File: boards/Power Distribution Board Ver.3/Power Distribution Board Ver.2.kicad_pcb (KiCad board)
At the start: 4 copper layers, 127 x 127 mm, 95 parts, among them J1 Screw_Terminal_01x02, J2 Screw_Terminal_01x06, J3 Screw_Terminal_01x06, J4 Screw_Terminal_01x06, K1 Relay, K2 Relay, K3 Relay, K4 Relay, K5 Relay, K6 Relay, SW1 SW_Push_Open, U1 SIC431AED-T1-GE3, U2 SIC431AED-T1-GE3, U3 SIC431AED-T1-GE3

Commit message: schematic changes
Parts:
- removed D1, D2, D3, D4, D5, D6: type="D" model="DIODE" lib="", Package_TO_SOT_SMD:TO-263-2
- removed the G*** at (79.4, 48.4)
- removed J2, J3: Screw_Terminal_01x06, power_board_support:12V terminal block
- removed K1, K2, K3, K4, K5, K6: Relay, power_board_support:A10 Relay
- removed SW1: SW_Push_Open, power_board_support:E-Stop
- added F1: 0685P9200-01, IRIS:FUSC3215X83N, F.Cu at (61.2, 123.4)
- added F2: 0685P9200-01, IRIS:FUSC3215X83N, F.Cu at (51.3, 123.7)
- added F3: 0685P9200-01, IRIS:FUSC3215X83N, F.Cu at (41.2, 123.7)
- moved REF** 63.4 mm to (77.2, 130.7)
- moved REF** 63.3 mm to (76.7, 27.1)
- moved D9 13.0 mm to (35.8, 114.4)
- moved D8 12.6 mm to (67.6, 114.4)
- moved D7 12.4 mm to (52.1, 114.4)
- moved C11 9.38 mm to (42.8, 74.8)
- moved C13 9.38 mm to (72.0, 65.9)
- moved C14 9.38 mm to (50.9, 66.0)
- moved C15 9.38 mm to (33.0, 66.0)
- moved C17 9.38 mm to (50.5, 79.8)
- moved C22 9.38 mm to (57.0, 101.9)
- moved C27 9.38 mm to (77.3, 101.9)
- moved C31 9.38 mm to (77.3, 87.8)
- moved C39 9.38 mm to (38.8, 101.9)
- moved C4 9.38 mm to (75.3, 69.7)
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- renumbered C19~C25 to C19, C21 to C20, C28 to C21, C29 to C22, C30 to C23, C31 to C24, C32 to C25, C22 to C26, C19 to C27, C23 to C28, C24 to C29, C25 to C30, C26 to C31, C26~C32 to C32, C33~C39 to C39
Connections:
- D7 pad 2: /5V_OUT_2 -> Net-(D7-K)
- D8 pad 2: /5V_OUT_3 -> Net-(D8-K)
- D9 pad 2: /5V_OUT_1 -> Net-(D9-K)
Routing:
- net /E-stop: track 177.1 -> 0.00 mm
- net /12V_IN_2: track 19.3 -> 0.00 mm
- net /12V_IN_3: track 18.9 -> 0.00 mm
- net /12V_IN_1: track 18.9 -> 0.00 mm
- net /12V_IN_4: track 13.3 -> 0.00 mm
- net /12V_IN_6: track 13.3 -> 0.00 mm
- net /12V_IN_5: track 13.3 -> 0.00 mm
- net Net-(D7-K): track 0.00 -> 10.2 mm
- net Net-(D5-A): track 8.59 -> 0.00 mm
- net Net-(D3-A): track 8.59 -> 0.00 mm
- net Net-(D1-A): track 8.59 -> 0.00 mm
- net /5V_OUT_3: track 14.6 -> 6.69 mm
- net /5V_OUT_2: track 13.5 -> 6.41 mm
- net /5V_OUT_1: track 13.1 -> 6.41 mm
- net Net-(D2-A): track 5.68 -> 0.00 mm
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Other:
- board outline removed
- board text removed: "Buffett Lee, Emily Lory, Joseph Hanger, Henry Lin, Ben Saarva, Jakub Wojdyla, Wyatt Sturn, Miaomiao Jin"

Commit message: PCBPCB Schematics Done
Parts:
- removed D7, D8, D9: type="D" model="DIODE" lib="", Package_TO_SOT_SMD:TO-263-2
- moved G*** 25.4 mm to (75.5, 89.5)
- moved F1 22.4 mm to (74.0, 105.0)
- moved F2 18.9 mm to (54.1, 105.0)
- moved F3 18.2 mm to (42.0, 105.5)
- moved REF** 16.0 mm to (80.0, 115.0)
- moved REF** 15.7 mm to (26.0, 115.0)
- moved J4 15.3 mm to (56.5, 116.5)
- moved REF** 5.00 mm to (80.0, 30.9)
- moved REF** 3.98 mm to (26.0, 30.9)
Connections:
- C16 pad 1: Net-(D8-A) -> Net-(U1-VOUT)
- C17 pad 1: Net-(D7-A) -> Net-(U2-VOUT)
- C18 pad 1: Net-(D9-A) -> Net-(U3-VOUT)
- C19 pad 1: Net-(D7-A) -> Net-(U2-VOUT)
- C20 pad 1: Net-(D7-A) -> Net-(U2-VOUT)
- C21 pad 1: Net-(D7-A) -> Net-(U2-VOUT)
- C22 pad 1: Net-(D7-A) -> Net-(U2-VOUT)
- C23 pad 1: Net-(D7-A) -> Net-(U2-VOUT)
- C24 pad 1: Net-(D7-A) -> Net-(U2-VOUT)
- C25 pad 1: Net-(D7-A) -> Net-(U2-VOUT)
- C26 pad 1: Net-(D8-A) -> Net-(U1-VOUT)
- C27 pad 1: Net-(D8-A) -> Net-(U1-VOUT)
- C28 pad 1: Net-(D8-A) -> Net-(U1-VOUT)
- C29 pad 1: Net-(D8-A) -> Net-(U1-VOUT)
- C30 pad 1: Net-(D8-A) -> Net-(U1-VOUT)
- C31 pad 1: Net-(D8-A) -> Net-(U1-VOUT)
- C32 pad 1: Net-(D8-A) -> Net-(U1-VOUT)
- C33 pad 1: Net-(D9-A) -> Net-(U3-VOUT)
- C34 pad 1: Net-(D9-A) -> Net-(U3-VOUT)
- C35 pad 1: Net-(D9-A) -> Net-(U3-VOUT)
- C36 pad 1: Net-(D9-A) -> Net-(U3-VOUT)
- C37 pad 1: Net-(D9-A) -> Net-(U3-VOUT)
- C38 pad 1: Net-(D9-A) -> Net-(U3-VOUT)
- C39 pad 1: Net-(D9-A) -> Net-(U3-VOUT)
- F1 pad 1: Net-(D8-K) -> Net-(U1-VOUT)
- F2 pad 1: Net-(D7-K) -> Net-(U2-VOUT)
- F3 pad 1: Net-(D9-K) -> Net-(U3-VOUT)
- L1 pad 2: Net-(D8-A) -> Net-(U1-VOUT)
- L2 pad 2: Net-(D7-A) -> Net-(U2-VOUT)
- L3 pad 2: Net-(D9-A) -> Net-(U3-VOUT)
- R22 pad 2: Net-(D8-A) -> Net-(U1-VOUT)
- R23 pad 2: Net-(D7-A) -> Net-(U2-VOUT)
- R24 pad 2: Net-(D9-A) -> Net-(U3-VOUT)
- U1 pad 18: Net-(D8-A) -> Net-(U1-VOUT)
- U2 pad 18: Net-(D7-A) -> Net-(U2-VOUT)
- U3 pad 18: Net-(D9-A) -> Net-(U3-VOUT)
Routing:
- net Net-(D8-A): track 54.0 -> 0.00 mm
- net Net-(D9-A): track 48.9 -> 0.00 mm
- net Net-(U3-VOUT): track 0.00 -> 47.6 mm
- net Net-(D7-A): track 46.9 -> 0.00 mm
- net Net-(U1-VOUT): track 0.00 -> 46.0 mm
- net Net-(U2-VOUT): track 0.00 -> 42.4 mm
- net Net-(D7-K): track 10.2 -> 0.00 mm
- net /5V_OUT_3: track 6.69 -> 14.2 mm
- net Net-(D8-K): track 5.15 -> 0.00 mm
- net Net-(D9-K): track 5.03 -> 0.00 mm
- net /5V_OUT_1: track 6.41 -> 10.4 mm
- net /5V_OUT_2: track 6.41 -> 10.1 mm
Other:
- board text added: "+"
- board text added: "IRIS - XV PCBPCB Ver. 3 Rev. A Henry Lin, Rina Manxhuka, Janine Zhu Ben Saarva, Wyatt Sturn, Arnav Rajesh, Jakub Wojdyla, Hriday Shah, Sakshi Singh, Medha Hariharan, Terry Wang, Vimalnath Selvam, Nihar Koganti, Andrew Bajek, Nakul Sivaraj"

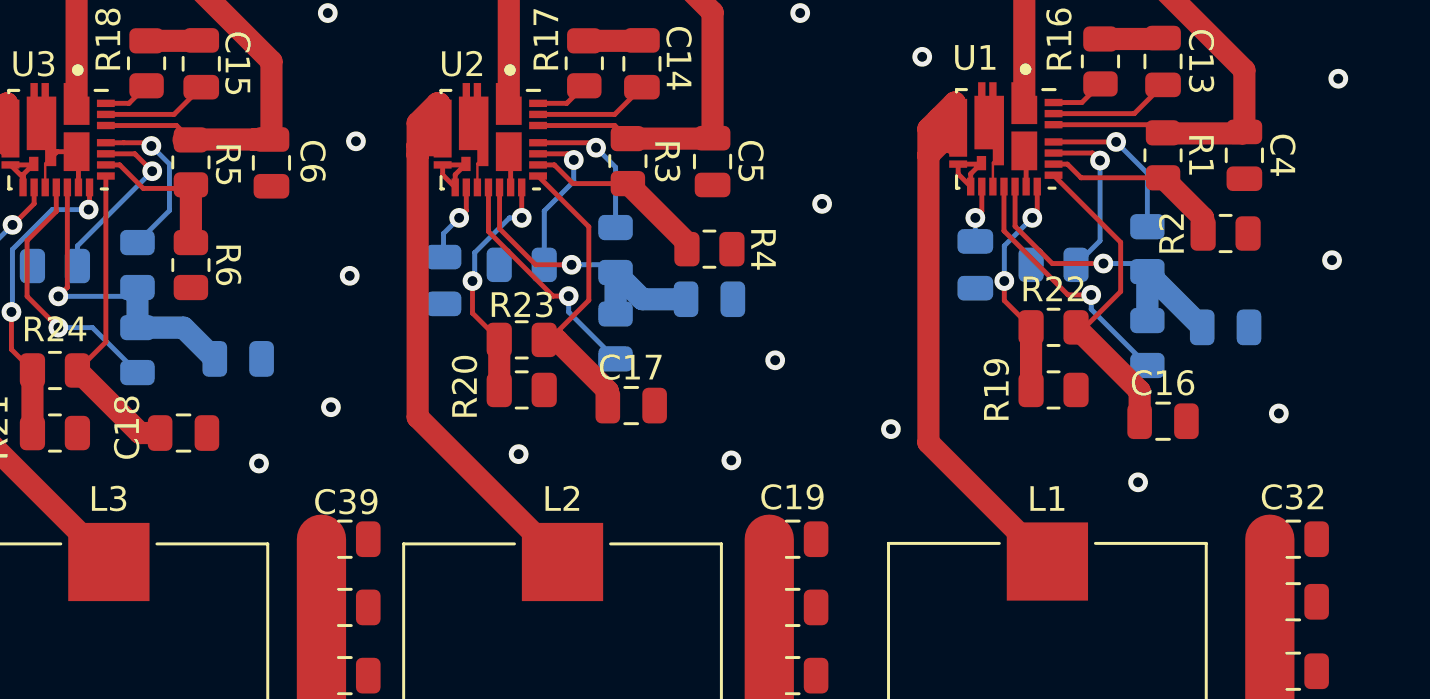
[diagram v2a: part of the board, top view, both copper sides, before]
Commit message: 12v relay footprint and updated board wiring
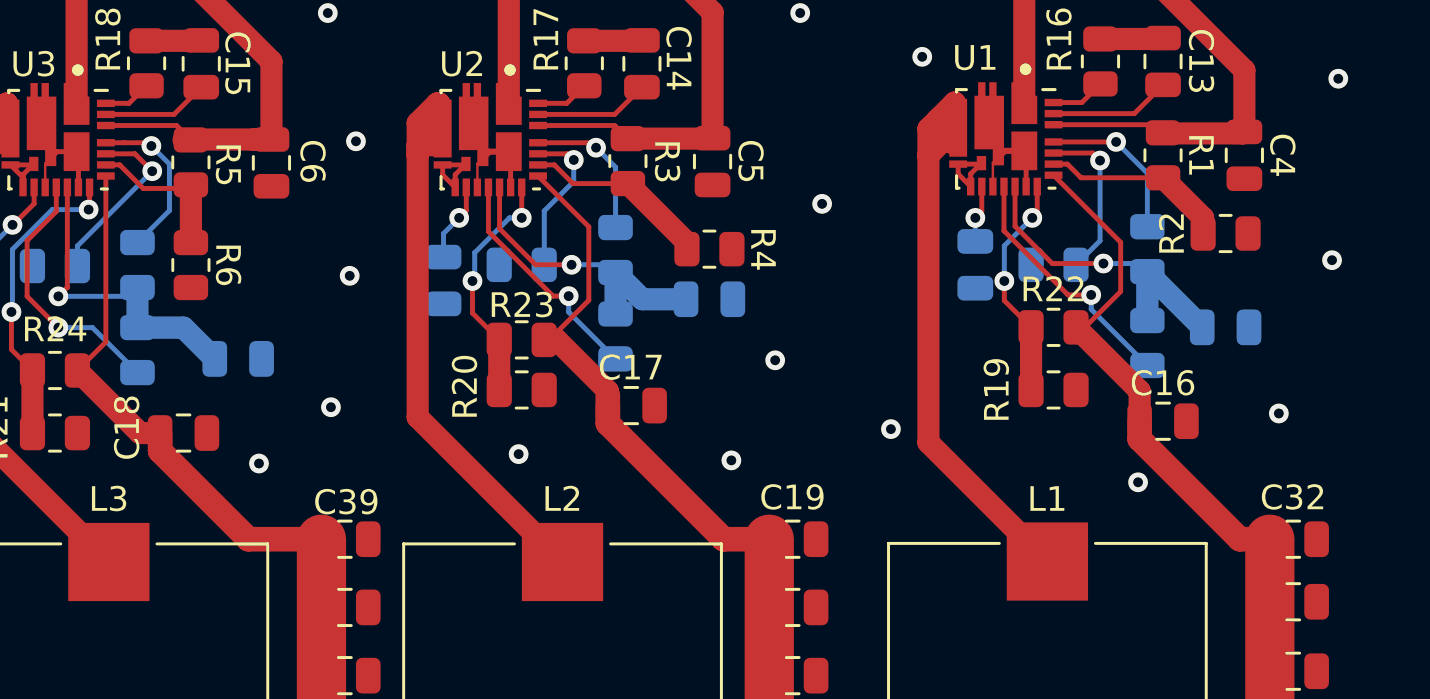
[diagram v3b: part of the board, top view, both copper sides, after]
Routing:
- net Net-(U2-VOUT): track 42.4 -> 51.6 mm
- net Net-(U3-VOUT): track 47.6 -> 56.4 mm
- net Net-(U1-VOUT): track 46.0 -> 53.7 mm
- net GND: track 9.44 -> 11.8 mm
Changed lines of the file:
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@@
+	)
+	(segment
+		(start 65.617845 69.507)
+		(end 65.355345 69.7695)
+		(width 0.25)
+		(layer "F.Cu")
+		(net 2)
+	)
+	(segment
+		(start 44.690345 69.5395)
+		(end 44.427845 69.802)
+		(width 0.25)
+		(layer "F.Cu")
+		(net 2)
 	)
 	(segment
@@
 	)
 	(segment
+		(start 66.407845 69.507)
+		(end 65.617845 69.507)
+		(width 0.25)
+		(layer "F.Cu")
+		(net 2)
+	)
+	(segment
 		(start 28.010345 70.9895)
 		(end 28.010345 69.6145)
@@
 		(net 2)
 	)
+	(segment
+		(start 45.480345 69.5395)
+		(end 44.690345 69.5395)
+		(width 0.25)
+		(layer "F.Cu")
+		(net 2)
+	)
 	(via
 		(at 53.3735 94.899)
@@
 	)
 	(segment
+		(start 71.090345 81.207)
+		(end 71.090345 80.482)
+		(width 1)
+		(layer "F.Cu")
+		(net 40)
+	)
+	(segment
 		(start 74.732725 103.53)
 		(end 76.375345 101.88738)
@@
 	)
 	(segment
+		(start 75.155345 85.272)
+		(end 71.090345 81.207)
+		(width 1)
+		(layer "F.Cu")
+		(net 40)
+	)
+	(segment
 		(start 68.865345 76.672)
 		(end 68.507845 76.672)
@@
 	)
 	(segment
+		(start 76.375345 85.272)
+		(end 75.155345 85.272)
+		(width 1)
+		(layer "F.Cu")
+		(net 40)
+	)
+	(segment
 		(start 54.16343 103.442725)
 		(end 54.5 103.442725)
@@
 	)
 	(segment
+		(start 56.055345 85.272)
+		(end 54.200345 85.272)
+		(width 1)
+		(layer "F.Cu")
+		(net 41)
+	)
+	(segment
 		(start 54.5 103.442725)
 		(end 56.055345 101.88738)
@@
 	)
 	(segment
+		(start 49.500345 80.572)
+		(end 49.500345 79.847)
+		(width 1)
+		(layer "F.Cu")
+		(net 41)
+	)
+	(segment
 		(start 48.729845 72.589)
 		(end 48.729845 75.57245)
@@
 	)
 	(segment
+		(start 54.200345 85.272)
+		(end 49.500345 80.572)
+		(width 1)
+		(layer "F.Cu")
+		(net 41)
+	)
+	(segment
 		(start 47.122295 77.18)
 		(end 46.917845 77.18)
@@
 	)
 	(segment
+		(start 31.325345 81.687)
+		(end 31.325345 80.962)
+		(width 1)
+		(layer "F.Cu")
+		(net 42)
+	)
+	(segment
 		(start 31.325345 80.962)
 		(end 30.507845 80.962)
@@
 	)
 	(segment
+		(start 37.875345 85.272)
+		(end 34.910345 85.272)
+		(width 1)
+		(layer "F.Cu")
+		(net 42)
+	)
+	(segment
 		(start 37.240345 97.627)
 		(end 37.875345 98.262)
@@
 		(layer "F.Cu")
 		(net 42)
+	)
+	(segment
+		(start 34.910345 85.272)
+		(end 31.325345 81.687)
+		(width 1)
+		(layer "F.Cu")
+		(net 42)
